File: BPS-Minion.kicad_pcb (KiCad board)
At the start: 2 copper layers, 85 x 152 mm, 219 parts, among them J10 TopConn, J11 TopConn, J2 BMS1OTP, J3 BMS2OTP, J4 Conn_01x24_Female, J5 Conn_01x24_Female, J6 TopConn, J7 TopConn, J8 TopConn, J9 TopConn, U10 LM321, U11 ADS7953SBDBT, U12 MIC5317-2.5xM5, U2 BQ7695201PFBR, U3 ISO1640BDR, U4 EL3H7, U5 BQ7695201PFBR, U6 ISO1640BDR, U7 EL3H7, U8 LM321, U9 ADS7953SBDBT

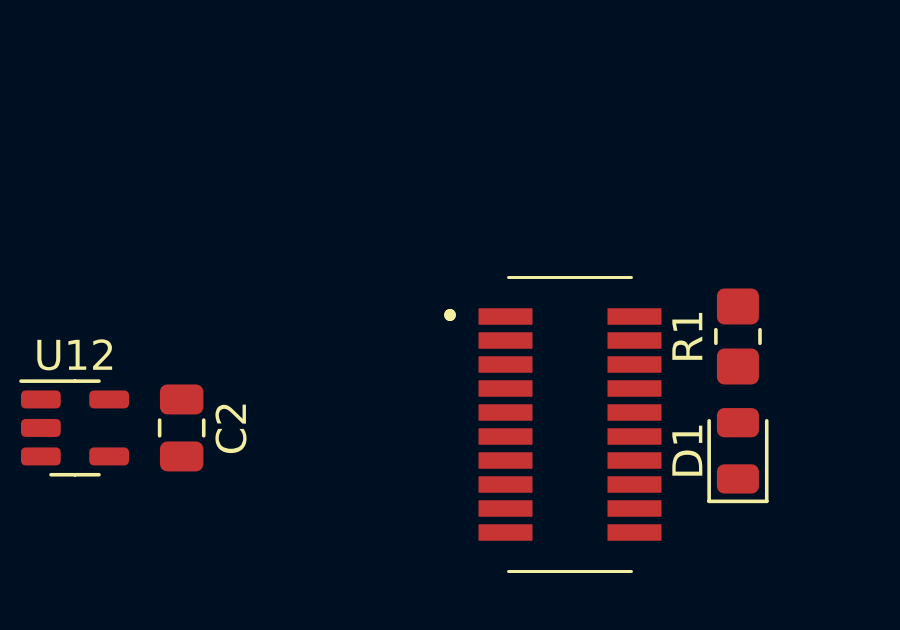
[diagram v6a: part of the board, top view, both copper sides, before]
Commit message: killed all the COMMONers
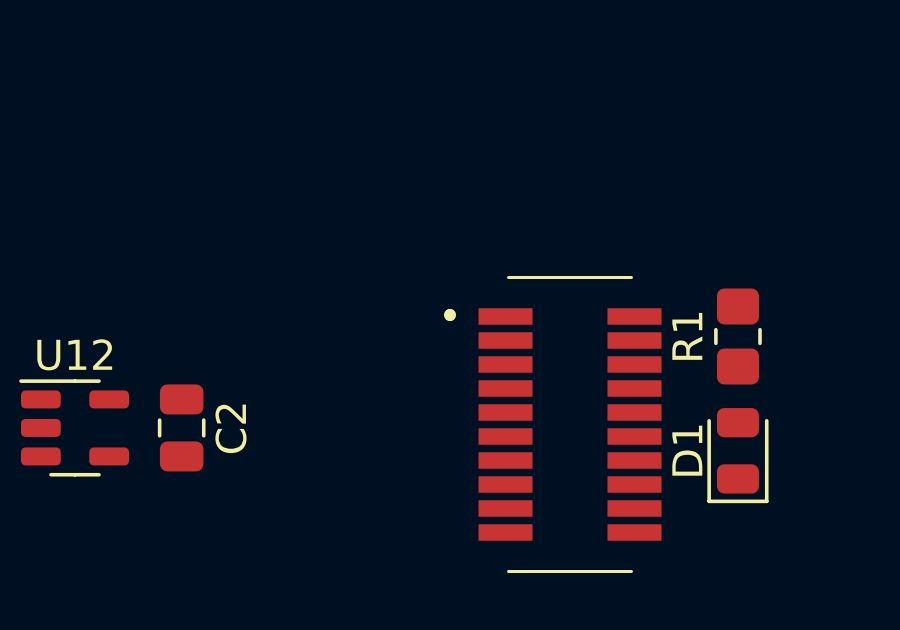
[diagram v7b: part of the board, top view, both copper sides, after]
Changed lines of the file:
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@@
     (pad "6" thru_hole oval (at 15 0 270) (size 1.5 2.02) (drill 1.02) (layers "*.Cu" "*.Mask")
       (net 71 "Net-(J9-Pin_6)") (pinfunction "Pin_6") (pintype "passive"))
-    (model "${KIPRJMOD}/common/utsvt3d/connectors.3dshapes/436500600.stp"
-      (offset (xyz 7.5 4 2))
+    (model "${KICAD6_3DMODEL_DIR}/Connector_Molex.3dshapes/Molex_Micro-Fit_3.0_43650-0600_1x06_P3.00mm_Horizontal.wrl"
+      (offset (xyz 0 0 0))
       (scale (xyz 1 1 1))
-      (rotate (xyz -90 0 -180))
+      (rotate (xyz 0 0 0))
     )
   )
@@
     (fp_line (start 14.45 5.071573) (end 18.55 5.071573)
       (stroke (width 0.1) (type solid)) (layer "F.SilkS"))
-    (fp_arc (start 12.5 -3.528427) (mid 12.55 -3.478427) (end 12.5 -3.428427)
+    (fp_arc (start 12.5 -3.528427) (mid 12.550027 -3.4784) (end 12.5 -3.428427)
       (stroke (width 0.3) (type solid)) (layer "F.SilkS"))
-    (fp_arc (start 12.5 -3.428427) (mid 12.45 -3.478427) (end 12.5 -3.528427)
+    (fp_arc (start 12.5 -3.428427) (mid 12.450027 -3.4784) (end 12.5 -3.528427)
       (stroke (width 0.3) (type solid)) (layer "F.SilkS"))
     (fp_line (start -20 21.171573) (end -20 -20.828427)
@@
     (fp_arc (start -16 25.171573) (mid -18.828427 24) (end -20 21.171573)
       (stroke (width 0.1) (type default)) (layer "Dwgs.User"))
-    (fp_arc (start 16 -24.828427) (mid 18.828427 -23.656854) (end 20 -20.828427)
+    (fp_arc (start 16 -24.828427) (mid 18.828437 -23.656856) (end 20 -20.828427)
       (stroke (width 0.1) (type default)) (layer "Dwgs.User"))
-    (fp_arc (start 20 21.171573) (mid 18.828427 24) (end 16 25.171573)
+    (fp_arc (start 20 21.171573) (mid 18.828426 23.999998) (end 16 25.171573)
       (stroke (width 0.1) (type default)) (layer "Dwgs.User"))
     (fp_circle (center 0 -20.828427) (end 3 -20.828427)
@@
     (pad "20" smd rect (at 18.65 3.771573 90) (size 0.55 1.8) (layers "F.Cu" "F.Paste" "F.Mask")
       (net 208 "unconnected-(U1-PA1(ADC)-Pad20)") (pinfunction "PA1(ADC)") (pintype "passive+no_connect"))
-    (group "" (id 0450eced-daa3-4a23-b2a2-75f46433921c)
+    (group "" (id e3a25eaf-9047-427c-8376-92775ba9b742)
       (members
-        00b25497-fb00-4230-b7f4-d19c8f37741e
-        05efd75e-8b7a-4388-913a-efa69a988b31
-        1c69a7ec-f958-4a22-937e-d7cdadf3b77f
-        240401b8-5ac8-457f-a38b-2b27697d49bd
-        60b252c1-84f6-461a-875d-687ef42b477b
-        66957630-fa7e-4aa5-8a7a-08f2eda6e6ce
-        80c09703-5026-4f67-9b77-d9409e6559f0
-        8a757254-e414-4e1c-83c3-49557fb29cd1
-        93e7184a-582e-4af1-bfb8-a92fa9c8badb
-        d0317508-6a7a-44bc-95eb-1275e3c3eecd
-        d978a8fd-5feb-4f47-8651-d22f8a4ac985
-        e0198e22-3894-44e1-ae7d-b59e338276e2
-        e9c90e77-d828-425e-8969-a78dfb43d3d3
+        1755b109-3f2a-4e06-9ffc-ba377fd1beab
+        2aee7c32-9267-42e8-8a44-82ef4eadd781
+        2d54b6c2-555e-4429-ad57-dd08a7d0fd33
+        32033943-e900-45e2-99e8-35ed0b069745
+        48180173-a5b4-41b2-9338-5bdd14d17701
+        49b14125-660b-421b-aa8d-98eaa1a19719
+        6c8ae2a1-1cd2-4b03-9e54-67c949169abe
+        a267c8ac-79ec-4e30-8990-9bcb7b117a92
+        aac42947-f8b6-4791-853e-93512bf5c25e
+        abd19cce-d795-4827-a031-89bb97212b16
+        b8ce8e8d-316a-498e-b062-d64aff13a698
+        bf0faaa5-037f-4488-9dd9-5a1a478c8347
+        ef65d4c2-e07c-4435-87c7-d8e79e7f102b
       )
     )
-    (group "" (id c19967fe-fe90-4d3e-a12d-28c6daf3582f)
+    (group "" (id 84adeed7-c0cf-4d2c-b85a-9fe5308e769f)
       (members
-        2bc34a0e-4cf5-48aa-82da-b986addc974e
-        965f9a71-dd32-422e-9df7-673b3c472b00
+        894c6f00-59ec-4a91-8164-eab41ab159ad
+        ace76c80-7821-467e-97fa-f41fdd77b06d
       )
     )
-    (model "${KIPRJMOD}/common/utsvt3d/connectors.3dshapes/53307-2071.stp"
+    (model "${KIPRJMOD}/UTSVT-KiCadLibraries/utsvt3d/connectors.3dshapes/53307-2071.stp"
       (offset (xyz 16.5 0.5 2))
       (scale (xyz 1 1 1))
       (rotate (xyz -90 0 -90))
     )
-    (model "${KIPRJMOD}/common/utsvt3d/misc.3dshapes/BPS-PeripheralSOM.step"
+    (model "${KIPRJMOD}/UTSVT-KiCadLibraries/utsvt3d/misc.3dshapes/BPS-PeripheralSOM.step"
       (offset (xyz 0 0 4.5))
       (scale (xyz 1 1 1))
@@
     (pad "6" thru_hole oval (at 15 0 270) (size 1.5 2.02) (drill 1.02) (layers "*.Cu" "*.Mask")
       (net 144 "Net-(J11-Pin_6)") (pinfunction "Pin_6") (pintype "passive"))
-    (model "${KIPRJMOD}/common/utsvt3d/connectors.3dshapes/436500600.stp"
-      (offset (xyz 7.5 4 2))
+    (model "${KICAD6_3DMODEL_DIR}/Connector_Molex.3dshapes/Molex_Micro-Fit_3.0_43650-0600_1x06_P3.00mm_Horizontal.wrl"
+      (offset (xyz 0 0 0))
       (scale (xyz 1 1 1))
-      (rotate (xyz -90 0 -180))
+      (rotate (xyz 0 0 0))
     )
   )
@@
     (pad "6" thru_hole oval (at 15 0 270) (size 1.5 2.02) (drill 1.02) (layers "*.Cu" "*.Mask")
       (net 8 "Net-(J7-Pin_6)") (pinfunction "Pin_6") (pintype "passive"))
-    (model "${KIPRJMOD}/common/utsvt3d/connectors.3dshapes/436500600.stp"
-      (offset (xyz 7.5 4.5 2))
+    (model "${KICAD6_3DMODEL_DIR}/Connector_Molex.3dshapes/Molex_Micro-Fit_3.0_43650-0600_1x06_P3.00mm_Horizontal.wrl"
+      (offset (xyz 0 0 0))
       (scale (xyz 1 1 1))
-      (rotate (xyz -90 0 -180))
+      (rotate (xyz 0 0 0))
     )
   )
@@
     (pad "6" thru_hole oval (at 15 0 270) (size 1.5 2.02) (drill 1.02) (layers "*.Cu" "*.Mask")
       (net 101 "Net-(J10-Pin_6)") (pinfunction "Pin_6") (pintype "passive"))
-    (model "${KIPRJMOD}/common/utsvt3d/connectors.3dshapes/436500600.stp"
-      (offset (xyz 7.5 3.5 2))
+    (model "${KICAD6_3DMODEL_DIR}/Connector_Molex.3dshapes/Molex_Micro-Fit_3.0_43650-0600_1x06_P3.00mm_Horizontal.wrl"
+      (offset (xyz 0 0 0))
       (scale (xyz 1 1 1))
-      (rotate (xyz -90 0 -180))
+      (rotate (xyz 0 0 0))
     )
   )
@@
     (pad "6" thru_hole oval (at 15 0 270) (size 1.5 2.02) (drill 1.02) (layers "*.Cu" "*.Mask")
       (net 14 "Net-(J8-Pin_6)") (pinfunction "Pin_6") (pintype "passive"))
-    (model "${KIPRJMOD}/common/utsvt3d/connectors.3dshapes/436500600.stp"
-      (offset (xyz 7.5 4 2))
+    (model "${KICAD6_3DMODEL_DIR}/Connector_Molex.3dshapes/Molex_Micro-Fit_3.0_43650-0600_1x06_P3.00mm_Horizontal.wrl"
+      (offset (xyz 0 0 0))
       (scale (xyz 1 1 1))
-      (rotate (xyz 90 -180 0))
+      (rotate (xyz 0 0 0))
     )
   )
@@
     (pad "6" thru_hole oval (at 15 0 270) (size 1.5 2.02) (drill 1.02) (layers "*.Cu" "*.Mask")
       (net 42 "Net-(J6-Pin_6)") (pinfunction "Pin_6") (pintype "passive"))
-    (model "${KIPRJMOD}/common/utsvt3d/connectors.3dshapes/436500600.stp"
-      (offset (xyz 7.5 4 2))
+    (model "${KICAD6_3DMODEL_DIR}/Connector_Molex.3dshapes/Molex_Micro-Fit_3.0_43650-0600_1x06_P3.00mm_Horizontal.wrl"
+      (offset (xyz 0 0 0))
       (scale (xyz 1 1 1))
-      (rotate (xyz -90 0 180))
+      (rotate (xyz 0 0 0))
     )
   )

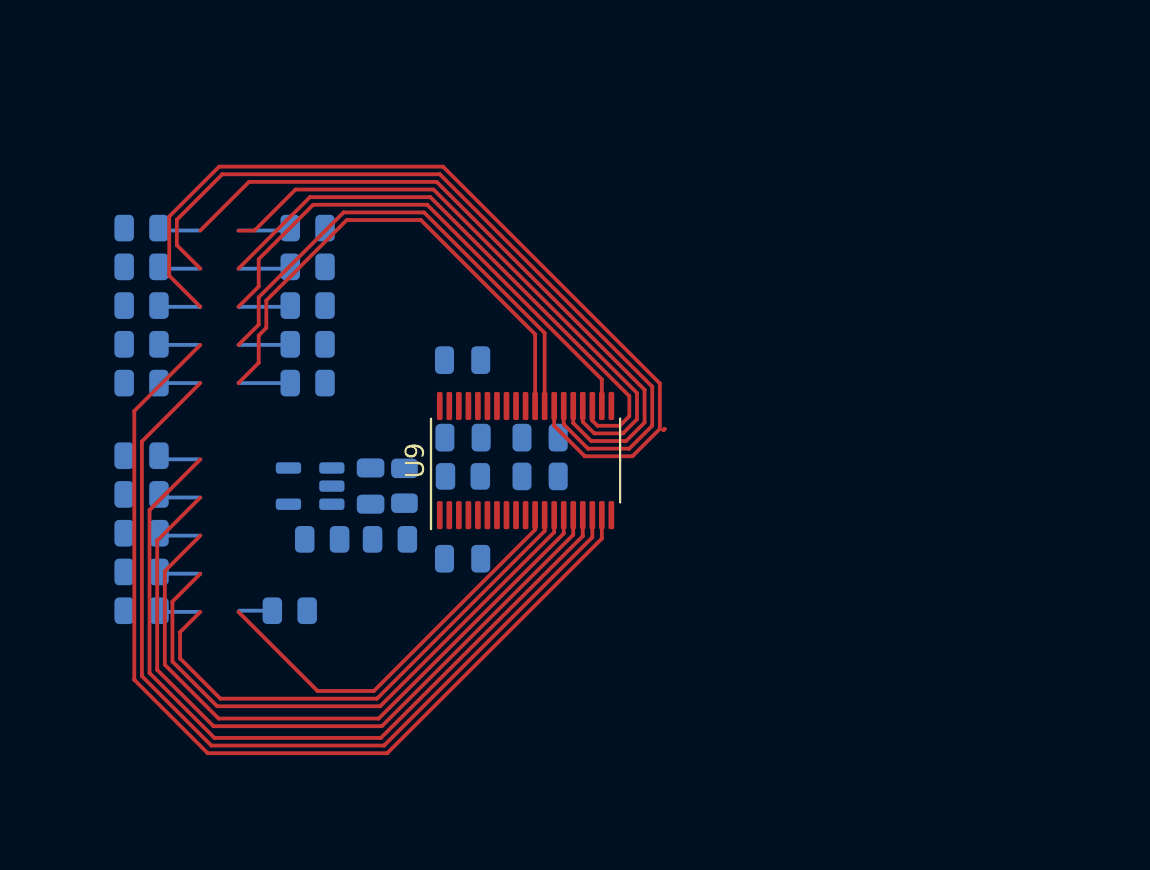
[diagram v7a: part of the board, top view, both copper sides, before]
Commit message: new ADC layout
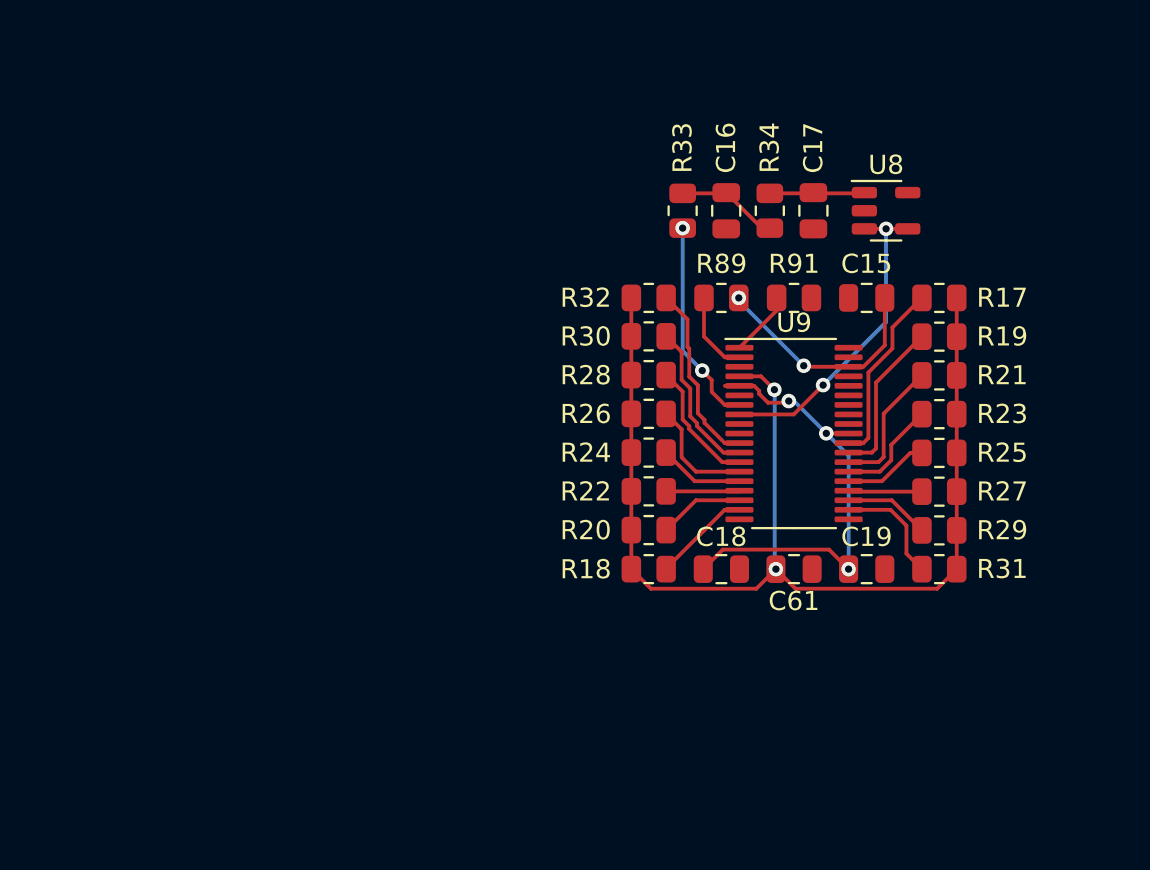
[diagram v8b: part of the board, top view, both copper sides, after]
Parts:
- C15, C16, C17, C18, C19, C61, R17, R18, R19, R20, R21, R22, R23, R24, R25, R26, R27, R28, R29, R30, R31, R32, R33, R34, R89, R91, U8: moved to F.Cu
- moved R25 43.5 mm to (10.7, 46.7), turned to 0 degrees
- moved R23 42.5 mm to (10.7, 44.7), turned to 0 degrees
- moved R21 42.0 mm to (10.7, 42.7), turned to 0 degrees
- moved R27 35.9 mm to (10.7, 48.8)
- moved R29 35.9 mm to (10.7, 50.8)
- moved R31 35.9 mm to (10.7, 52.8)
- moved U8 33.5 mm to (7.87, 34.0), turned to 0 degrees
- moved R17 33.4 mm to (10.7, 38.6)
- moved R19 33.1 mm to (10.7, 40.6)
- moved R30 30.2 mm to (-4.57, 40.6)
- moved R18 29.1 mm to (-4.57, 52.8)
- moved R28 28.5 mm to (-4.57, 42.7)
- moved R20 27.7 mm to (-4.57, 50.8)
- moved C17 27.3 mm to (4.06, 34.0)
- moved R26 27.3 mm to (-4.57, 44.7)
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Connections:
- C16 pad 1: GND -> GNDA
- C17 pad 1: GND -> GNDA
- C21 pad 1: GND -> GNDA
- C22 pad 1: GND -> GNDA
- U10 pad 2: GND -> GNDA
- U8 pad 2: GND -> GNDA
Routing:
- net +2V5: track 0.00 -> 58.8 mm, vias 0 -> 2
- net /Temperature/temp9: track 53.2 -> 5.16 mm
- net /Temperature/temp10: track 49.6 -> 4.49 mm
- net /Temperature/temp3: track 49.4 -> 7.06 mm
- net /Temperature/temp11: track 44.2 -> 3.86 mm
- net /Temperature/temp4: track 44.5 -> 5.57 mm
- net /Temperature/temp12: track 40.4 -> 4.47 mm
- net /Temperature/temp5: track 38.2 -> 4.46 mm
- net /Temperature/temp13: track 36.8 -> 5.96 mm
- net /Temperature/temp6: track 34.6 -> 3.86 mm
- net /Temperature/temp7: track 33.2 -> 4.50 mm
- net /Temperature/temp14: track 33.1 -> 6.68 mm
- net /Temperature/temp8: track 30.0 -> 5.99 mm
- net VDDA: track 0.00 -> 23.8 mm, vias 0 -> 3
- net /Temperature/temp15: track 29.5 -> 8.18 mm
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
